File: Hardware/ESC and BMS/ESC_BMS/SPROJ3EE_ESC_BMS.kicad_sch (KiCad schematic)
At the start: 0 parts

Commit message: initial BMS work
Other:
- note added: "A"
- note added: "A1"
- note added: "A2"
- note added: "B"
- note added: "B+"
- note added: "B-"
- note added: "B1"
- note added: "B2"
- note added: "BMid"
- note added: "BQ2962"
- note added: "Battery Config"
- note added: "V1"
- note added: "V2"
- note added: "V3"
- note added: "and"

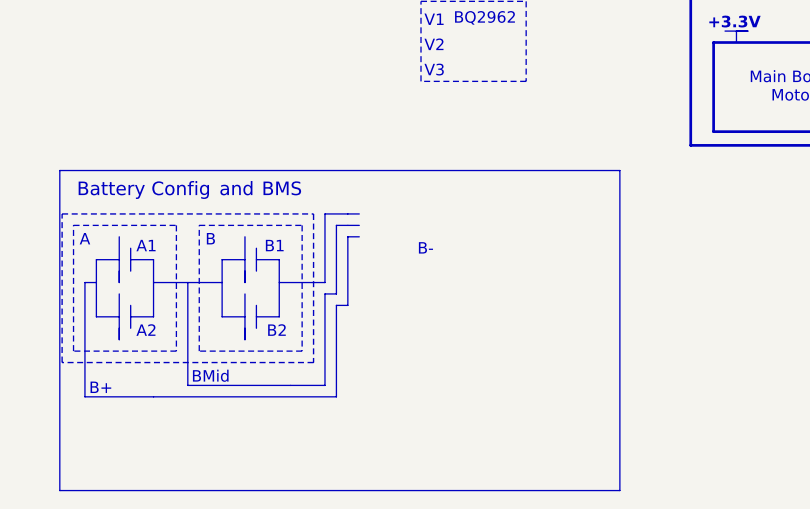
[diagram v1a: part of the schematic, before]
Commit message: some more BMS work + fixed RP2040 XIN/XOUT shortage
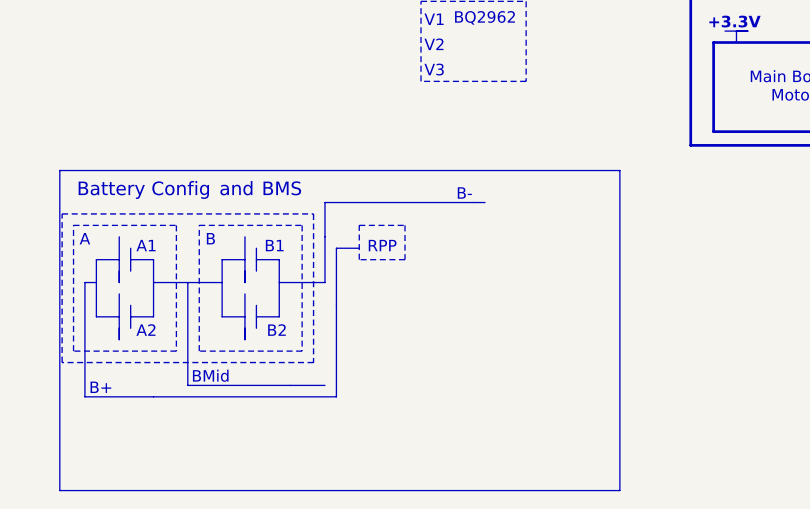
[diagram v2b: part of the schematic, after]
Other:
- note added: "RPP"
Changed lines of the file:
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@@
+	)
+	(rectangle
+		(start 50.8 64.77)
+		(end 55.88 68.58)
+		(stroke
+			(width 0)
+			(type dash)
+			(color 46 63 255 1)
+		)
+		(fill
+			(type none)
+		)
 	)
 	(rectangle
@@
 	(text "B-"
 		(exclude_from_sim no)
-		(at 58.166 67.564 0)
+		(at 62.484 61.468 0)
 		(effects
 			(font
@@
 		)
 	)
+	(text "RPP"
+		(exclude_from_sim no)
+		(at 53.34 67.31 0)
+		(effects
+			(font
+				(size 1.27 1.27)
+				(color 46 63 255 1)
+			)
+		)
+	)
 	(text "Block diagram of the schematic"
 		(exclude_from_sim no)
@@
 	(polyline
 		(pts
-			(xy 49.53 73.66) (xy 49.53 66.04)
+			(xy 48.26 73.66) (xy 48.26 67.31)
 		)
 		(stroke
@@
 	(polyline
 		(pts
-			(xy 48.26 72.39) (xy 48.26 64.77)
-		)
-		(stroke
-			(width 0)
-			(type solid)
-		)
-	)
-	(polyline
-		(pts
 			(xy 41.91 68.58) (xy 41.91 74.93)
 		)
@@
 	(polyline
 		(pts
-			(xy 49.53 63.5) (xy 50.8 63.5)
+			(xy 63.5 62.23) (xy 64.77 62.23)
 		)
 		(stroke
@@
 	(polyline
 		(pts
-			(xy 48.26 64.77) (xy 49.53 64.77)
-		)
-		(stroke
-			(width 0)
-			(type solid)
-		)
-	)
-	(polyline
-		(pts
 			(xy 27.94 68.58) (xy 27.94 74.93)
 		)
@@
 	(polyline
 		(pts
+			(xy 46.99 62.23) (xy 46.99 66.04)
+		)
+		(stroke
+			(width 0)
+			(type default)
+		)
+	)
+	(polyline
+		(pts
 			(xy 21.59 74.93) (xy 24.13 74.93)
 		)
@@
 	(polyline
 		(pts
-			(xy 49.53 64.77) (xy 50.8 64.77)
-		)
-		(stroke
-			(width 0)
-			(type solid)
-		)
-	)
-	(polyline
-		(pts
 			(xy 137.16 36.83) (xy 137.16 43.18)
 		)
@@
 	(polyline
 		(pts
-			(xy 46.99 82.55) (xy 46.99 72.39)
-		)
-		(stroke
-			(width 0)
-			(type solid)
-		)
-	)
-	(polyline
-		(pts
 			(xy 25.4 67.31) (xy 25.4 69.85)
 		)
@@
 	(polyline
 		(pts
-			(xy 49.53 66.04) (xy 50.8 66.04)
+			(xy 48.26 67.31) (xy 50.8 67.31)
 		)
 		(stroke
@@
 	(polyline
 		(pts
-			(xy 46.99 63.5) (xy 49.53 63.5)
+			(xy 46.99 62.23) (xy 63.5 62.23)
 		)
 		(stroke
@@
 	(polyline
 		(pts
-			(xy 48.26 73.66) (xy 49.53 73.66)
+			(xy 48.26 73.66) (xy 48.26 73.66)
 		)
 		(stroke
@@
 	(polyline
 		(pts
-			(xy 46.99 71.12) (xy 46.99 63.5)
+			(xy 46.99 71.12) (xy 46.99 66.04)
 		)
 		(stroke
@@
 		)
 	)
-	(polyline
-		(pts
-			(xy 46.99 72.39) (xy 48.26 72.39)
-		)
-		(stroke
-			(width 0)
-			(type solid)
-		)
-	)

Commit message: BMS almost full
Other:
- note added: "+VPROT"
- note added: "BQ2969T"
- note added: "Balancing"
- note added: "Charging"
- note added: "GND"
- note added: "OCP"
- note added: "OVP"
- note added: "Protections + BMS"
- note added: "UVP"
- note removed: "BQ2962"
- note removed: "V1"
- note removed: "V2"
- note removed: "V3"

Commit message: more BMS
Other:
- sheet 1. ECS renamed 1. ESC
- note added: "CHARGER"
- note added: "J11"
- note added: "J12"
- note added: "J13"
- note added: "J14"

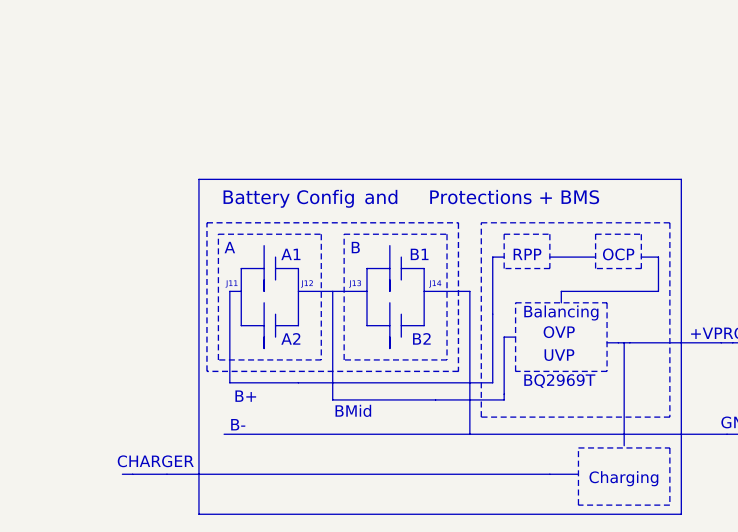
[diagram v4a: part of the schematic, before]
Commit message: Simulations for BMS start and footprints
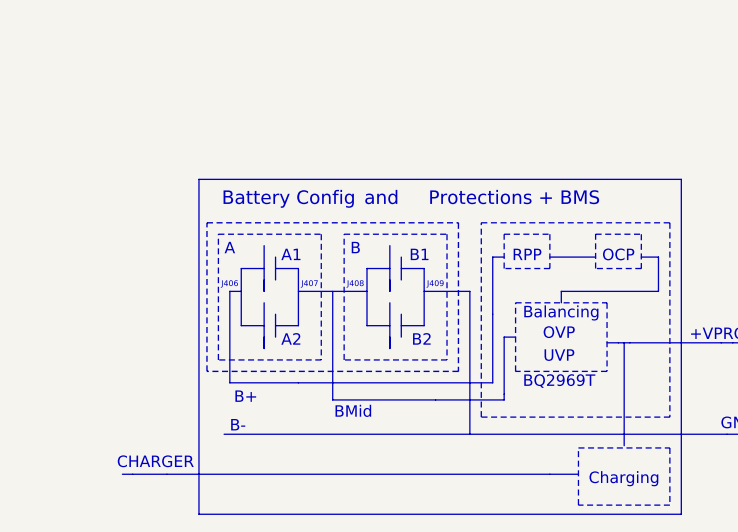
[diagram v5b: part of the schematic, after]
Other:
- note added: "J406"
- note added: "J407"
- note added: "J408"
- note added: "J409"
- note removed: "J11"
- note removed: "J12"
- note removed: "J13"
- note removed: "J14"
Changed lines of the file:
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@@
 		)
 	)
-	(text "J14"
+	(text "J409"
 		(exclude_from_sim no)
 		(at 53.34 77.47 0)
@@
 		)
 	)
-	(text "J11"
+	(text "J406"
 		(exclude_from_sim no)
-		(at 30.734 77.47 0)
+		(at 30.48 77.47 0)
 		(effects
 			(font
@@
 		)
 	)
-	(text "J12"
+	(text "J407\n"
 		(exclude_from_sim no)
-		(at 39.116 77.47 0)
+		(at 39.37 77.47 0)
 		(effects
 			(font
@@
 		)
 	)
-	(text "J13"
+	(text "J408"
 		(exclude_from_sim no)
 		(at 44.45 77.47 0)

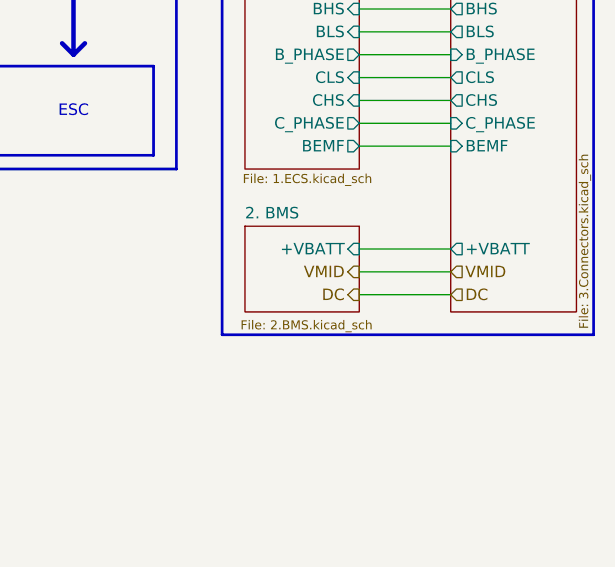
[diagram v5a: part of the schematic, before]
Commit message: ESC BMS component placement close to done
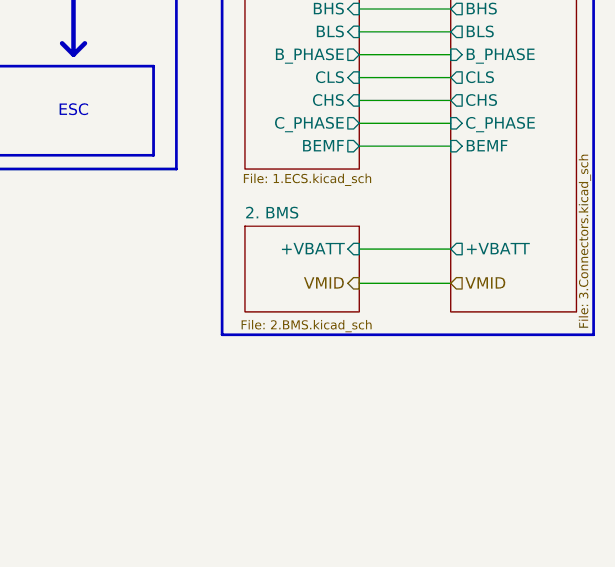
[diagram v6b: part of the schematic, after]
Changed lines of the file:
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@@
-		)
-	)
-	(wire
-		(pts
-			(xy 168.91 69.85) (xy 179.07 69.85)
-		)
-		(stroke
-			(width 0)
-			(type default)
 		)
 	)
@@
 	(wire
 		(pts
-			(xy 168.91 67.31) (xy 179.07 67.31)
+			(xy 168.91 68.58) (xy 179.07 68.58)
 		)
 		(stroke
@@
 	(hierarchical_label "VMID"
 		(shape output)
-		(at 168.91 67.31 180)
+		(at 168.91 68.58 180)
 		(effects
 			(font
@@
 		)
 	)
-	(hierarchical_label "DC"
+	(hierarchical_label "VMID"
 		(shape input)
-		(at 179.07 69.85 0)
+		(at 179.07 68.58 0)
 		(effects
 			(font
@@
 		)
 	)
-	(hierarchical_label "VMID"
-		(shape input)
-		(at 179.07 67.31 0)
-		(effects
-			(font
-				(size 1.27 1.27)
-			)
-			(justify left)
-		)
-	)
-	(hierarchical_label "DC"
-		(shape output)
-		(at 168.91 69.85 180)
-		(effects
-			(font
-				(size 1.27 1.27)
-			)
-			(justify right)
-		)
-	)

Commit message: ESC done
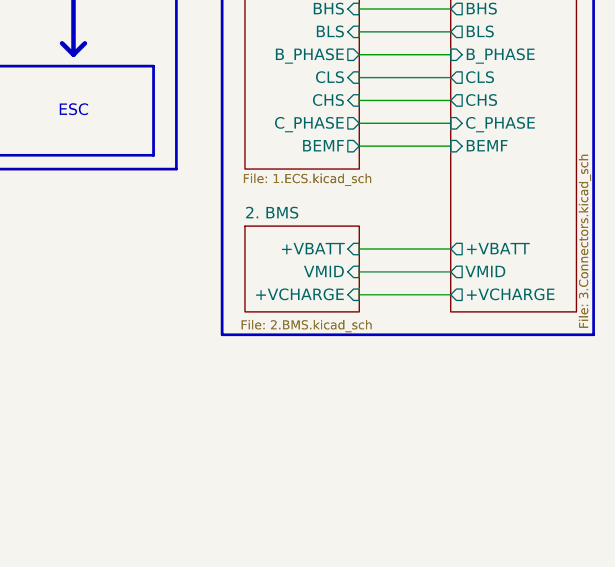
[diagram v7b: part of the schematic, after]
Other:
- sheet 2. BMS ports: added +VCHARGE, VMID; removed none
- sheet 3. Connectors ports: added +VCHARGE, VMID; removed none
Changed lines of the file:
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@@
+		)
+	)
+	(wire
+		(pts
+			(xy 168.91 69.85) (xy 179.07 69.85)
+		)
+		(stroke
+			(width 0)
+			(type default)
 		)
 	)
@@
 	(wire
 		(pts
-			(xy 168.91 68.58) (xy 179.07 68.58)
+			(xy 168.91 67.31) (xy 179.07 67.31)
 		)
 		(stroke
@@
 			(width 0)
 			(type default)
-		)
-	)
-	(hierarchical_label "VMID"
-		(shape output)
-		(at 168.91 68.58 180)
-		(effects
-			(font
-				(size 1.27 1.27)
-			)
-			(justify right)
-		)
-	)
-	(hierarchical_label "VMID"
-		(shape input)
-		(at 179.07 68.58 0)
-		(effects
-			(font
-				(size 1.27 1.27)
-			)
-			(justify left)
 		)
 	)
@@
 			)
 		)
+		(pin "VMID" output
+			(at 179.07 67.31 180)
+			(effects
+				(font
+					(size 1.27 1.27)
+				)
+				(justify left)
+			)
+		)
+		(pin "+VCHARGE" output
+			(at 179.07 69.85 180)
+			(effects
+				(font
+					(size 1.27 1.27)
+				)
+				(justify left)
+			)
+		)
 		(instances
 			(project "SPROJ3EE_ESC_BMS"
@@
 			(effects
 				(font
+					(size 1.27 1.27)
+				)
+				(justify right)
+			)
+		)
+		(pin "VMID" input
+			(at 168.91 67.31 0)
+			(effects
+				(font
+					(size 1.27 1.27)
+				)
+				(justify right)
+			)
+		)
+		(pin "+VCHARGE" input
+			(at 168.91 69.85 0)
+			(effects
+				(font

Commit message: Small adjustments
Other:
- note added: "BQ2969"
- note removed: "+Vprot"
- note removed: "BQ2969T"
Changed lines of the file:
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@@
 		)
 	)
-	(text "+Vprot"
+	(text "+VPROT"
 		(exclude_from_sim no)
 		(at 143.002 23.114 0)
@@
 		)
 	)
-	(text "BQ2969T"
+	(text "BQ2969"
 		(exclude_from_sim no)
 		(at 67.056 88.265 0)
